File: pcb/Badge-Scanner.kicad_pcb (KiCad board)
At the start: 2 copper layers, 73 x 52 mm, 72 parts, among them J1 NFC-Module, J2 Serial, J3 I2C, J4 Micro_SD_Card_Det1, M1 Fan, Q1 AO3400A, Q2 AO3401A, Q3 AO3401A, Q4 AO3401A, Q5 AO3400A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

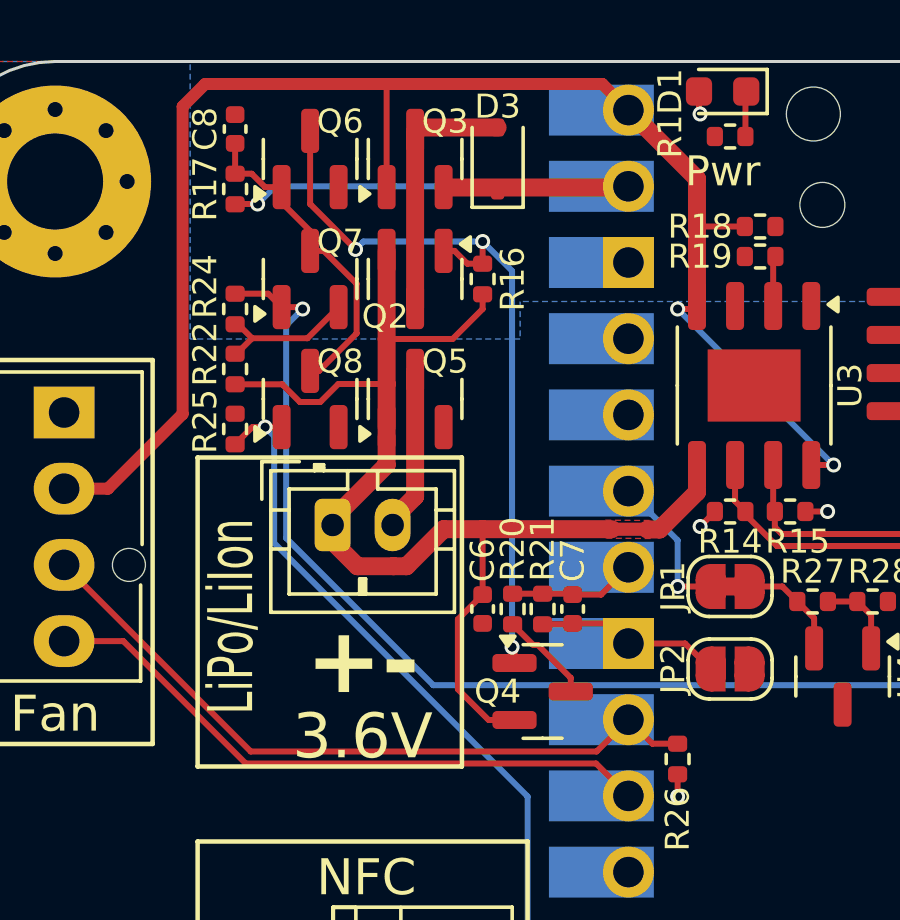
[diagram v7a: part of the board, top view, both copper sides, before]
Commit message: fix: move measurement to BattSwd
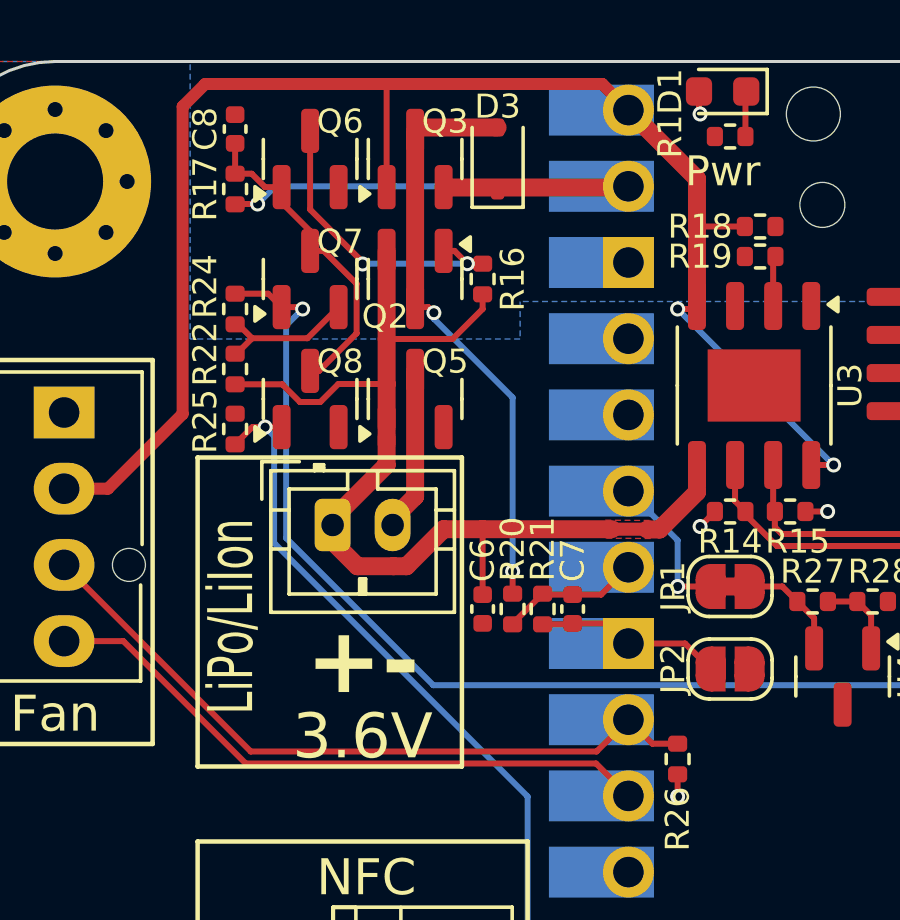
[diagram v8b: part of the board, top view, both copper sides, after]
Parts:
- removed Q4: AO3401A, Package_TO_SOT_SMD:SOT-23
- turned R20 to -90 degrees
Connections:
- R20 pad 1: Net-(Q4-D) -> /Battery Management/BattSwd
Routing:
- net /Battery Management/BattSwG: track 25.6 -> 10.1 mm, vias 3 -> 2
- net /Battery Management/BattSwd: track 8.67 -> 19.8 mm, vias 0 -> 2
- net /Battery Management/Batt+: track 42.5 -> 36.7 mm
- net Net-(Q4-D): track 3.13 -> 0.00 mm
